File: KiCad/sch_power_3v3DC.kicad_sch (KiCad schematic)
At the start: 6 parts, among them U1 TLV75533PDBVR

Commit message: Update BoM
Update components with full description and Digikey P/N.
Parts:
- D1: Digikey_PN (none) -> 732-4978-1-ND
- R1: footprint Resistor_SMD:R_0603_1608Metric_Pad0.98x0.95mm_HandSolder -> Resistor_SMD:R_0603_1608Metric
- S1: Digikey_PN (none) -> 401-1999-1-ND
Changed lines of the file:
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@@
+			)
+		)
+		(property "Sim.Device" ""
+			(at 129.54 58.42 0)
+			(effects
+				(font
+					(size 1.27 1.27)
+				)
+			)
+		)
+		(property "Sim.Library" ""
+			(at 129.54 58.42 0)
+			(effects
+				(font
+					(size 1.27 1.27)
+				)
+			)
+		)
+		(property "Sim.Name" ""
+			(at 129.54 58.42 0)
+			(effects
+				(font
+					(size 1.27 1.27)
+				)
+			)
+		)
+		(property "Sim.Params" ""
+			(at 129.54 58.42 0)
+			(effects
+				(font
+					(size 1.27 1.27)
+				)
+			)
+		)
+		(property "Sim.Pins" ""
+			(at 129.54 58.42 0)
+			(effects
+				(font
+					(size 1.27 1.27)
+				)
 			)
 		)
@@
 				)
 				(hide yes)
+			)
+		)
+		(property "Sim.Device" ""
+			(at 144.78 58.42 0)
+			(effects
+				(font
+					(size 1.27 1.27)
+				)
+			)
+		)
+		(property "Sim.Library" ""
+			(at 144.78 58.42 0)
+			(effects
+				(font
+					(size 1.27 1.27)
+				)
+			)
+		)
+		(property "Sim.Name" ""
+			(at 144.78 58.42 0)
+			(effects
+				(font
+					(size 1.27 1.27)
+				)
+			)
+		)
+		(property "Sim.Params" ""
+			(at 144.78 58.42 0)
+			(effects
+				(font
+					(size 1.27 1.27)
+				)
+			)
+		)
+		(property "Sim.Pins" ""
+			(at 144.78 58.42 0)
+			(effects
+				(font
+					(size 1.27 1.27)
+				)
 			)
 		)
@@
 			)
 		)
-		(property "Footprint" "Resistor_SMD:R_0603_1608Metric_Pad0.98x0.95mm_HandSolder"
+		(property "Footprint" "Resistor_SMD:R_0603_1608Metric"
 			(at 175.26 95.25 0)
 			(effects
@@
 			)
 		)
-		(property "Description" "Resistor, small US symbol"
+		(property "Description" "4.7 kOhms ±5% 0.1W, 1/10W Chip Resistor 0603 (1608 Metric) Thick Film"
 			(at 175.26 95.25 0)
 			(effects
@@
 				)
 				(hide yes)
+			)
+		)
+		(property "Sim.Pins" ""
+			(at 175.26 95.25 0)
+			(effects
+				(font
+					(size 1.27 1.27)
+				)
 			)
 		)
@@
 				)
 				(hide yes)
+			)
+		)
+		(property "Sim.Device" ""
+			(at 114.3 60.96 0)
+			(effects
+				(font
+					(size 1.27 1.27)
+				)
+			)
+		)
+		(property "Sim.Library" ""
+			(at 114.3 60.96 0)
+			(effects
+				(font
+					(size 1.27 1.27)
+				)
+			)
+		)
+		(property "Sim.Name" ""
+			(at 114.3 60.96 0)
+			(effects
+				(font
+					(size 1.27 1.27)
+				)
+			)
+		)
+		(property "Sim.Params" ""
+			(at 114.3 60.96 0)
+			(effects
+				(font
+					(size 1.27 1.27)
+				)
+			)
+		)
+		(property "Sim.Pins" ""
+			(at 114.3 60.96 0)
+			(effects
+				(font
+					(size 1.27 1.27)
+				)
 			)
 		)
@@
 			)
 		)
-		(property "Description" "Light emitting diode"
-			(at 175.26 102.87 0)
-			(effects
-				(font
-					(size 1.27 1.27)
-				)
-				(hide yes)
-			)
-		)
-		(property "Sim.Pins" "1=K 2=A"
+		(property "Description" "Red 625nm LED Indication - Discrete 2V 0603 (1608 Metric)"
 			(at 175.26 102.87 0)
 			(effects
@@
 			)
 		)
-		(property "Digikey_PN" ""
+		(property "Digikey_PN" "732-4978-1-ND"
 			(at 175.26 102.87 0)
 			(effects
@@
 				)
 				(hide yes)
+			)
+		)
+		(property "Sim.Pins" ""
+			(at 175.26 102.87 0)
+			(effects
+				(font
+					(size 1.27 1.27)
+				)
 			)
 		)
@@
 			)
 		)
-		(property "Description" ""
+		(property "Description" "Slide Switch SPDT Surface Mount, Right Angle, 300mA, 6V"
 			(at 187.96 53.34 0)
 			(effects
@@
 			)
 		)
-		(property "Digikey_PN" ""
+		(property "Digikey_PN" "401-1999-1-ND"
 			(at 187.96 53.34 0)
 			(effects
@@
 			)
 		)
+		(property "Sim.Device" ""
+			(at 187.96 53.34 0)
+			(effects
+				(font
+					(size 1.27 1.27)
+				)
+			)
+		)
+		(property "Sim.Library" ""
+			(at 187.96 53.34 0)
+			(effects
+				(font
+					(size 1.27 1.27)
+				)
+			)
+		)
+		(property "Sim.Name" ""
+			(at 187.96 53.34 0)
+			(effects
+				(font
+					(size 1.27 1.27)
+				)
+			)
+		)
+		(property "Sim.Params" ""
+			(at 187.96 53.34 0)
+			(effects
+				(font
+					(size 1.27 1.27)
+				)
+			)
+		)
+		(property "Sim.Pins" ""
+			(at 187.96 53.34 0)
+			(effects
+				(font
+					(size 1.27 1.27)
+				)
+			)
+		)

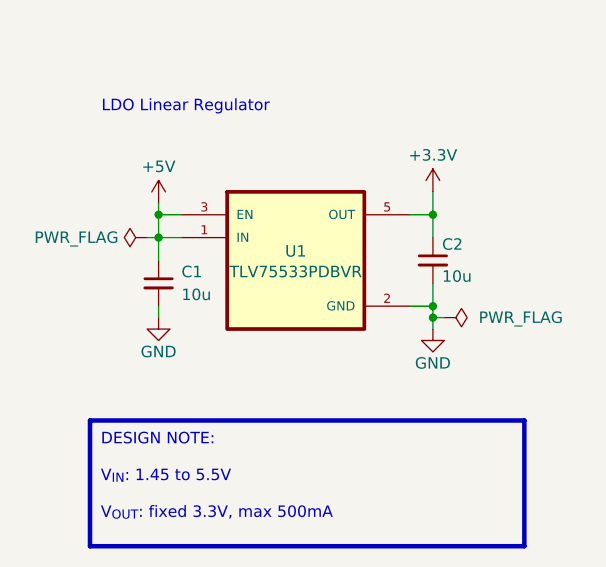
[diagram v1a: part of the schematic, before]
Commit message: Update BOM and general tidy-up
Include DigiKey cut-tape components and add flag to indicate own stocked items. Remove files that aren't part of the sharable project (KiCad 9 embeds), Remove empty/irrelevant folders.
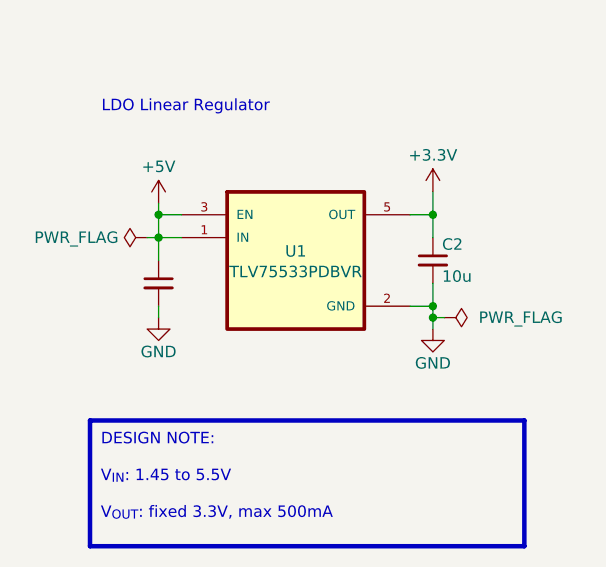
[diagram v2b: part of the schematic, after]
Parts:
- C1, C2, D1, R1: Stocked (none) -> Yes
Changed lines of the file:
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@@
+			)
+		)
+		(property "Stocked" "Yes"
+			(at 144.78 58.42 0)
+			(effects
+				(font
+					(size 1.27 1.27)
+				)
+				(hide yes)
+			)
+		)
+		(property "Silk" ""
+			(at 144.78 58.42 0)
+			(effects
+				(font
+					(size 1.27 1.27)
+				)
+				(hide yes)
 			)
 		)
@@
 			)
 		)
-		(property "Supplier" ""
-			(at 175.26 95.25 0)
-			(effects
-				(font
-					(size 1.27 1.27)
-				)
-				(hide yes)
-			)
-		)
 		(property "Digikey_PN" "541-3993-1-ND"
 			(at 175.26 95.25 0)
@@
 			)
 		)
-		(property "Sim.Pins" ""
-			(at 175.26 95.25 0)
-			(effects
-				(font
-					(size 1.27 1.27)
-				)
+		(property "Stocked" "Yes"
+			(at 175.26 95.25 0)
+			(effects
+				(font
+					(size 1.27 1.27)
+				)
+				(hide yes)
+			)
+		)
+		(property "Silk" ""
+			(at 175.26 95.25 0)
+			(effects
+				(font
+					(size 1.27 1.27)
+				)
+				(hide yes)
 			)
 		)
@@
 				)
 				(justify left)
+				(hide yes)
 			)
 		)
@@
 				)
 				(justify left)
+				(hide yes)
 			)
 		)
@@
 					(size 1.27 1.27)
 				)
+				(hide yes)
 			)
 		)
@@
 					(size 1.27 1.27)
 				)
+				(hide yes)
 			)
 		)
@@
 					(size 1.27 1.27)
 				)
+				(hide yes)
 			)
 		)
@@
 					(size 1.27 1.27)
 				)
+				(hide yes)
 			)
 		)
@@
 					(size 1.27 1.27)
 				)
+				(hide yes)
+			)
+		)
+		(property "Stocked" "Yes"
+			(at 114.3 60.96 0)
+			(effects
+				(font
+					(size 1.27 1.27)
+				)
+				(hide yes)
+			)
+		)
+		(property "Silk" ""
+			(at 114.3 60.96 0)
+			(effects
+				(font
+					(size 1.27 1.27)
+				)
+				(hide yes)
 			)
 		)
@@
 			)
 		)
-		(property "Sim.Pins" ""
-			(at 175.26 102.87 0)
-			(effects
-				(font
-					(size 1.27 1.27)
-				)
-			)
-		)
+		(property "Stocked" "Yes"
+			(at 175.26 102.87 0)
+			(effects
+				(font
+					(size 1.27 1.27)
+				)
+				(hide yes)
+			)
+		)
